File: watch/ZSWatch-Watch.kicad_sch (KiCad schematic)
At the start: 0 parts

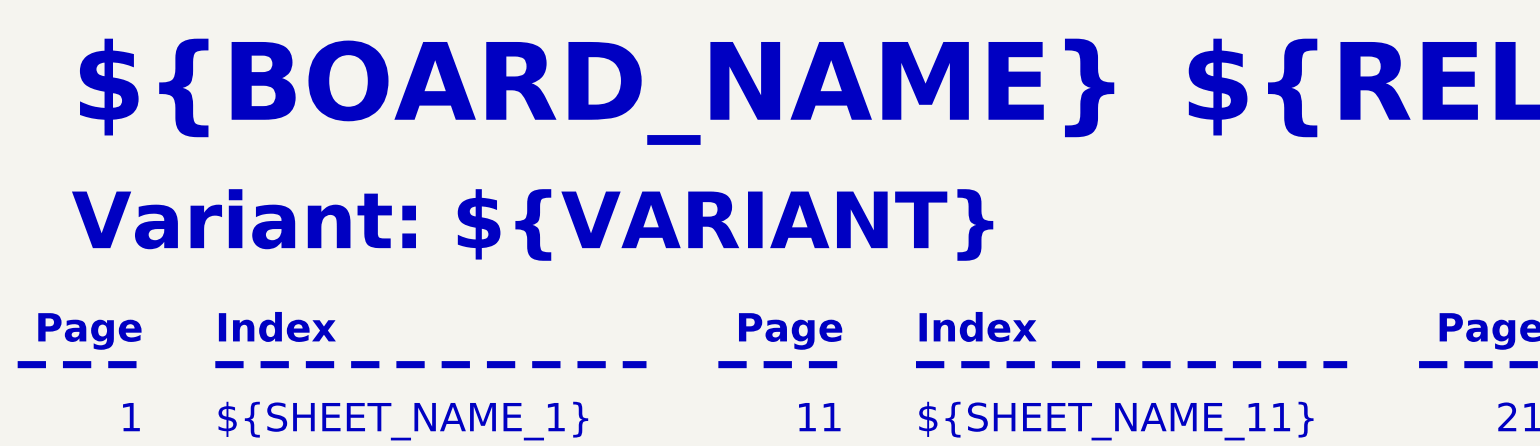
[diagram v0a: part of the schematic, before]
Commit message: Update to the latest KiCad template and KiCad 10
- Port schematics, layout and the local libraries to the KiCad 10 file format
  (ERC/DRC unchanged), rename the text variable VARIANT to PCB_VARIANT and use
  KICAD10_3DMODEL_DIR for the 3D models
- Replace watch.yaml and changelog-check.yaml with the template workflows
  hw-pcb.yaml and common-changelog.yaml (KiCad 10 image, BoM check, Mouser cart,
  release and GitHub Pages deployment). The pinned kicad-library submodule is kept
- Remove the committed production outputs and CI logs, they are attached to the
  release and published on GitHub Pages instead
- Update the KiBot configuration, resources and title block templates from the
  template, keep the project values and the release entries
- Add the create-dev-branch and create-release skills and the CI scripts

Co-Authored-By: Claude Opus 5.5 <noreply@anthropic.com>
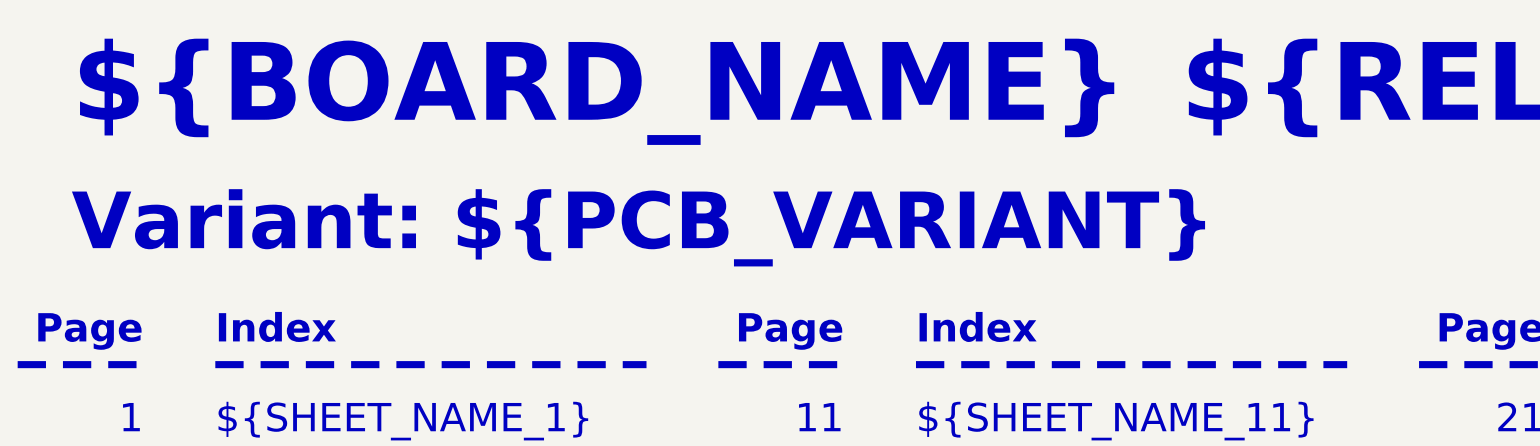
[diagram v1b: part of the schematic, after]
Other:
- note added: "Variant: ${PCB_VARIANT}"
- note removed: "Variant: ${VARIANT}"
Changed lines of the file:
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@@
 (kicad_sch
-	(version 20250114)
+	(version 20260306)
 	(generator "eeschema")
-	(generator_version "9.0")
+	(generator_version "10.0")
 	(paper "A3")
 	(title_block
@@
 		(company "${COMPANY}")
 	)
-	(text "Variant: ${VARIANT}"
+	(text "Variant: ${PCB_VARIANT}"
 		(exclude_from_sim no)
 		(at 31.75 59.69 0)
@@
 		)
 		(fill
-			(color 0 0 0 0.0000)
+			(color 0 0 0 0)
 		)
 		(property "Sheetname" "Revision History"
 			(at 346.71 302.26 0)
+			(show_name no)
+			(do_not_autoplace no)
 			(effects
 				(font
@@
 		(property "Sheetfile" "Revision History.kicad_sch"
 			(at 347.345 304.8 0)
+			(show_name no)
+			(do_not_autoplace no)
 			(effects
 				(font
@@
 		)
 		(fill
-			(color 0 0 0 0.0000)
+			(color 0 0 0 0)
 		)
 		(property "Sheetname" "Power - Topology"
 			(at 306.07 315.2009 0)
+			(show_name no)
+			(do_not_autoplace no)
 			(effects
 				(font
@@
 		(property "Sheetfile" "Power - Topology.kicad_sch"
 			(at 307.34 317.5 0)
+			(show_name no)
+			(do_not_autoplace no)
 			(effects
 				(font
@@
 		)
 		(fill
-			(color 0 0 0 0.0000)
+			(color 0 0 0 0)
 		)
 		(property "Sheetname" "Block Diagram"
 			(at 306.07 302.5009 0)
+			(show_name no)
+			(do_not_autoplace no)
 			(effects
 				(font
@@
 		(property "Sheetfile" "Block Diagram.kicad_sch"
 			(at 307.34 304.8 0)
+			(show_name no)
+			(do_not_autoplace no)
 			(effects
 				(font
@@
 		)
 		(fill
-			(color 0 0 0 0.0000)
+			(color 0 0 0 0)
 		)
 		(property "Sheetname" "Project Architecture"
 			(at 346.71 315.2009 0)
+			(show_name no)
+			(do_not_autoplace no)
 			(effects
 				(font
@@
 		(property "Sheetfile" "Project Architecture.kicad_sch"
 			(at 347.98 317.5 0)
+			(show_name no)
+			(do_not_autoplace no)
 			(effects
 				(font
@@
 		)
 	)
-	(embedded_fonts no)
 )

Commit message: Update schematic and layout with KiCad 10
Changes to the MCU and Power sheets and the layout, saved with KiCad 10
(adds the new KiCad 10 project settings).

Co-Authored-By: Claude Opus 5.5 <noreply@anthropic.com>
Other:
- note added: "Revision ${REVISION}"
- note removed: "Rev ${REVISION}"
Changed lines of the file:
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@@
 		)
 	)
-	(text "Rev ${REVISION}"
+	(text "Revision ${REVISION}"
 		(exclude_from_sim no)
 		(at 394.97 59.69 0)
@@
 		)
 	)
+	(embedded_fonts no)
 )

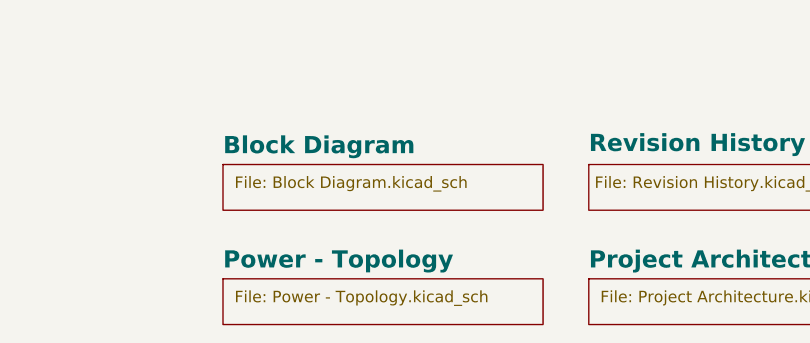
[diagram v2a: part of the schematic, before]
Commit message: Fix DRC errors and remove the Power - Topology sheet
Fixes the annular width of the mounting holes of S501 to S504 and the
courtyard overlaps of J1 with C403 and X509. The removed sheet also fixes the
duplicate page number 2.

Co-Authored-By: Claude Opus 5.5 <noreply@anthropic.com>
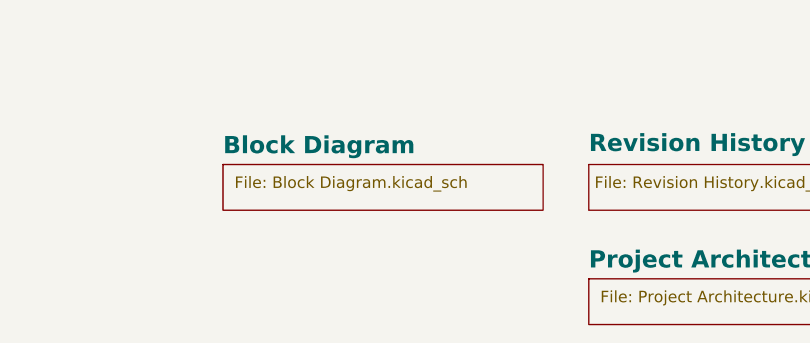
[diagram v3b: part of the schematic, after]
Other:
- removed sheet Power - Topology
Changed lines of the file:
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@@
-	)
-	(sheet
-		(at 306.07 316.23)
-		(size 35.56 5.08)
-		(exclude_from_sim no)
-		(in_bom yes)
-		(on_board yes)
-		(dnp no)
-		(stroke
-			(width 0.1524)
-			(type solid)
-		)
-		(fill
-			(color 0 0 0 0)
-		)
-		(property "Sheetname" "Power - Topology"
-			(at 306.07 315.2009 0)
-			(show_name no)
-			(do_not_autoplace no)
-			(effects
-				(font
-					(face "Times New Roman")
-					(size 1.905 1.905)
-					(bold yes)
-					(color 0 0 0 1)
-				)
-				(justify left bottom)
-			)
-		)
-		(property "Sheetfile" "Power - Topology.kicad_sch"
-			(at 307.34 317.5 0)
-			(show_name no)
-			(do_not_autoplace no)
-			(effects
-				(font
-					(face "Arial")
-					(size 1.27 1.27)
-				)
-				(justify left top)
-			)
-		)
-		(instances
-			(project "ZSWatch-Watch"
-				(path "/d5742f03-3b1a-42e5-a384-018bd4b919aa"
-					(page "2")
-				)
-			)
-		)
 	)
 	(sheet
